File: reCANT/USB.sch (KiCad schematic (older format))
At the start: 15 parts, among them J1 USB_C_Receptacle_USB2.0, U1 USB3343, U10 DSC1001

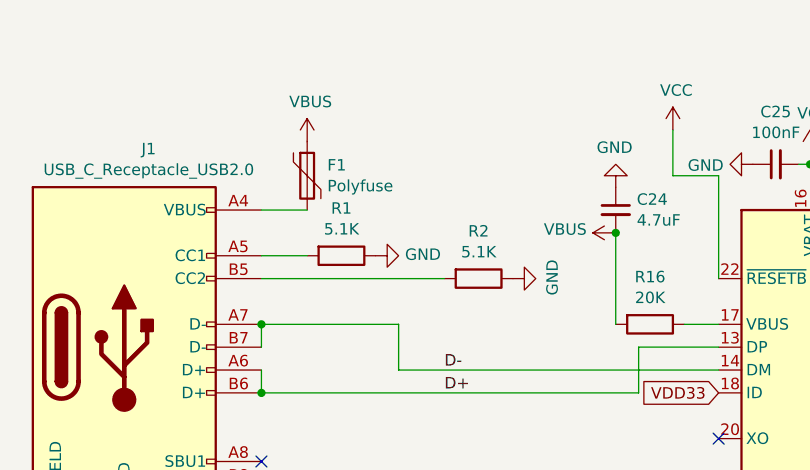
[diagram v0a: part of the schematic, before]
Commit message: Add LCSC part numbers for each component. Not that chipocalypse makes building this right now feasible...
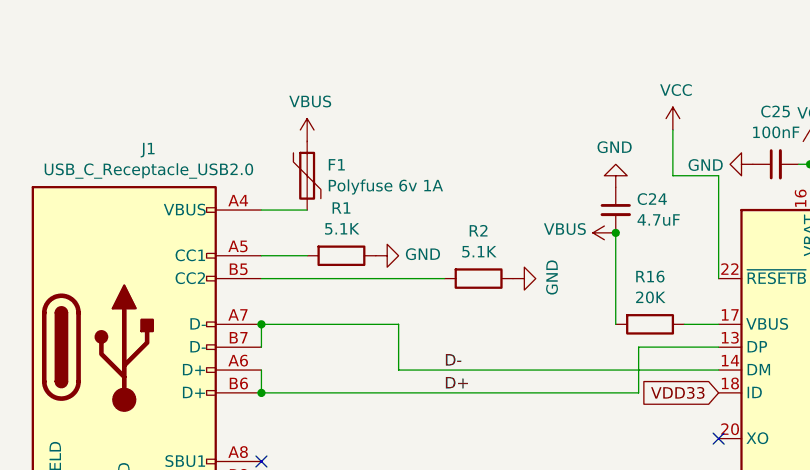
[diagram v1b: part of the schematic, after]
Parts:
- C1, C26, C27: LCSC (none) -> C28323
- C24: LCSC (none) -> C1779
- C25, C28, C29: LCSC (none) -> C49678
- F1: value Polyfuse -> Polyfuse 6v 1A; LCSC (none) -> C207022
- R1, R2: LCSC (none) -> C27834
- R16: LCSC (none) -> C4328
- R17: LCSC (none) -> C19006
- U1: LCSC (none) -> C112967
- U10: LCSC (none) -> C409249
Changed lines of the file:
@@
 P 2200 1200
 F 0 "F1" H 2288 1246 50  0000 L CNN
-F 1 "Polyfuse" H 2288 1155 50  0000 L CNN
+F 1 "Polyfuse 6v 1A" H 2288 1155 50  0000 L CNN
 F 2 "Capacitor_SMD:C_0805_2012Metric" H 2250 1000 50  0001 L CNN
 F 3 "~" H 2200 1200 50  0001 C CNN
+F 4 "C207022" H 2200 1200 50  0001 C CNN "LCSC"
 	1    2200 1200
 	1    0    0    -1
@@
 F 2 "Resistor_SMD:R_0805_2012Metric" V 2280 1550 50  0001 C CNN
 F 3 "~" H 2350 1550 50  0001 C CNN
+F 4 "C27834" V 2350 1550 50  0001 C CNN "LCSC"
 	1    2350 1550
 	0    1    1    0
@@
 F 2 "Resistor_SMD:R_0805_2012Metric" V 2880 1650 50  0001 C CNN
 F 3 "~" H 2950 1650 50  0001 C CNN
+F 4 "C27834" V 2950 1650 50  0001 C CNN "LCSC"
 	1    2950 1650
 	0    1    1    0
@@
 F 2 "Capacitor_SMD:C_0805_2012Metric" H 850 3050 50  0001 C CNN
 F 3 "~" H 850 3050 50  0001 C CNN
+F 4 "C28323" V 850 3050 50  0001 C CNN "LCSC"
 	1    850  3050
 	0    -1   -1   0
@@
 F 2 "Resistor_SMD:R_0805_2012Metric" V 3780 2850 50  0001 C CNN
 F 3 "~" H 3850 2850 50  0001 C CNN
+F 4 "C19006" V 3850 2850 50  0001 C CNN "LCSC"
 	1    3850 2850
 	0    1    1    0
@@
 F 2 "Capacitor_SMD:C_0805_2012Metric" H 3550 1350 50  0001 C CNN
 F 3 "~" H 3550 1350 50  0001 C CNN
+F 4 "C1779" H 3550 1350 50  0001 C CNN "LCSC"
 	1    3550 1350
 	1    0    0    -1
@@
 F 2 "Resistor_SMD:R_0805_2012Metric" V 3630 1850 50  0001 C CNN
 F 3 "~" H 3700 1850 50  0001 C CNN
+F 4 "C4328" V 3700 1850 50  0001 C CNN "LCSC"
 	1    3700 1850
 	0    1    1    0
@@
 F 2 "Capacitor_SMD:C_0805_2012Metric" H 4250 1150 50  0001 C CNN
 F 3 "~" H 4250 1150 50  0001 C CNN
+F 4 "C49678" V 4250 1150 50  0001 C CNN "LCSC"
 	1    4250 1150
 	0    -1   -1   0
@@
 F 2 "Capacitor_SMD:C_0805_2012Metric" H 4700 1050 50  0001 C CNN
 F 3 "~" H 4700 1050 50  0001 C CNN
+F 4 "C28323" V 4700 1050 50  0001 C CNN "LCSC"
 	1    4700 1050
 	0    -1   -1   0
@@
 F 2 "Capacitor_SMD:C_0805_2012Metric" H 5200 1200 50  0001 C CNN
 F 3 "~" H 5200 1200 50  0001 C CNN
+F 4 "C28323" V 5200 1200 50  0001 C CNN "LCSC"
 	1    5200 1200
 	0    1    1    0
@@
 F 2 "Package_DFN_QFN:QFN-24-1EP_4x4mm_P0.5mm_EP2.6x2.6mm" H 5100 2350 50  0001 C CNN
 F 3 "http://ww1.microchip.com/downloads/en/DeviceDoc/334x.pdf" H 5100 2450 50  0001 C CNN
+F 4 "C112967" H 4600 2150 50  0001 C CNN "LCSC"
 	1    4600 2150
 	1    0    0    -1
@@
 F 2 "DSC1001:Oscillator_SMD_Microchip_DSC1001-4Pin_2.5x2.0mm" H 2700 3350 50  0001 C CNN
 F 3 "https://abracon.com/Oscillators/ASDMB.pdf" H 3000 3800 50  0001 C CNN
+F 4 "C409249" H 2700 3350 50  0001 C CNN "LCSC"
 	1    2700 3350
 	1    0    0    -1
@@
 F 2 "Capacitor_SMD:C_0805_2012Metric" H 5750 1500 50  0001 C CNN
 F 3 "~" H 5750 1500 50  0001 C CNN
+F 4 "C49678" H 5750 1500 50  0001 C CNN "LCSC"
 	1    5750 1500
 	1    0    0    -1
@@
 F 2 "Capacitor_SMD:C_0805_2012Metric" H 2600 2900 50  0001 C CNN
 F 3 "~" H 2600 2900 50  0001 C CNN
+F 4 "C49678" V 2600 2900 50  0001 C CNN "LCSC"
 	1    2600 2900
 	0    1    1    0

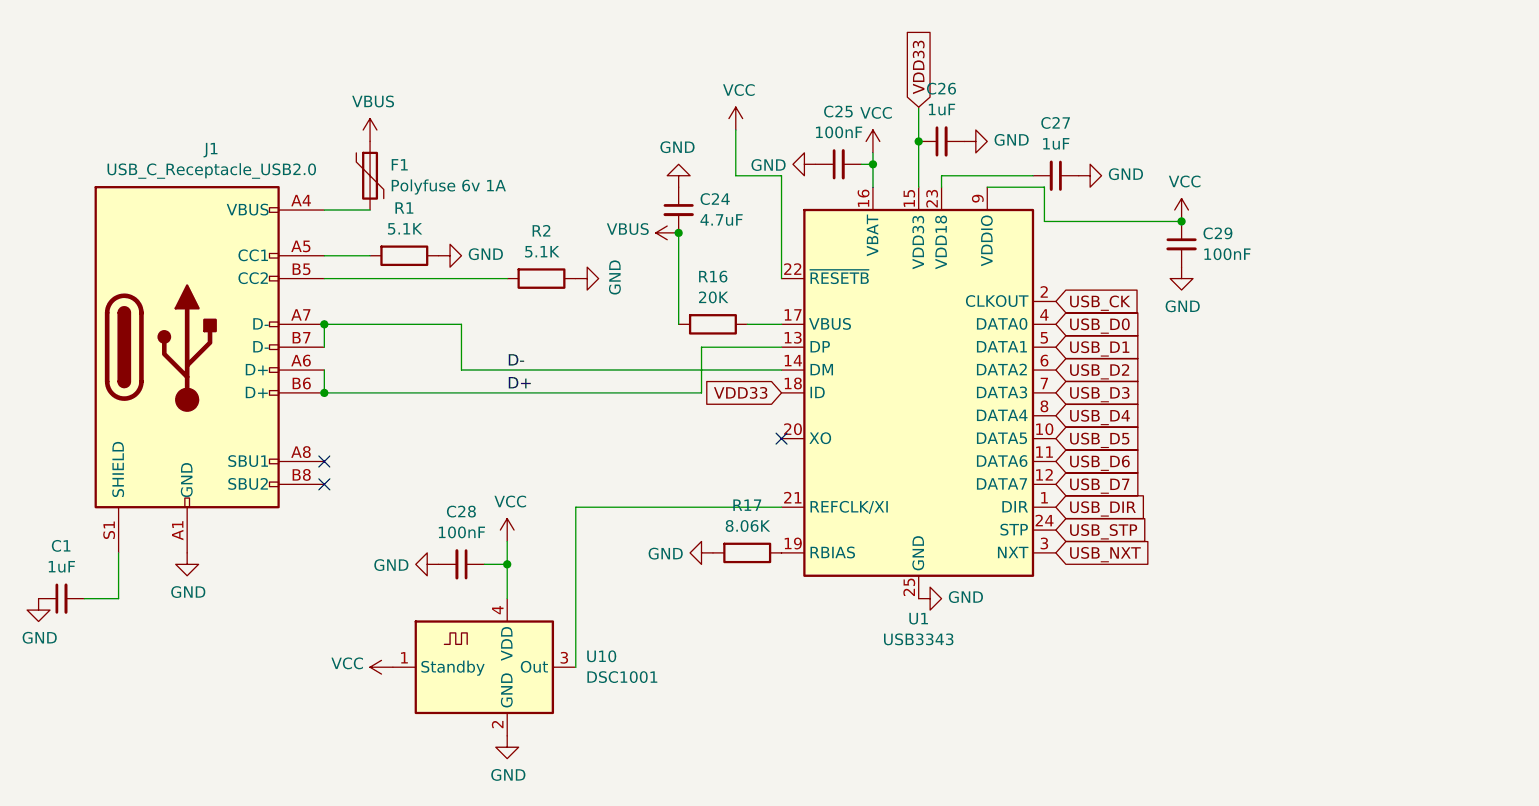
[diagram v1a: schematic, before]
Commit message: Added test points for debugging USB. Fixed impedence on USB traces to be correct for JLCPCBs JLC7628 buildup
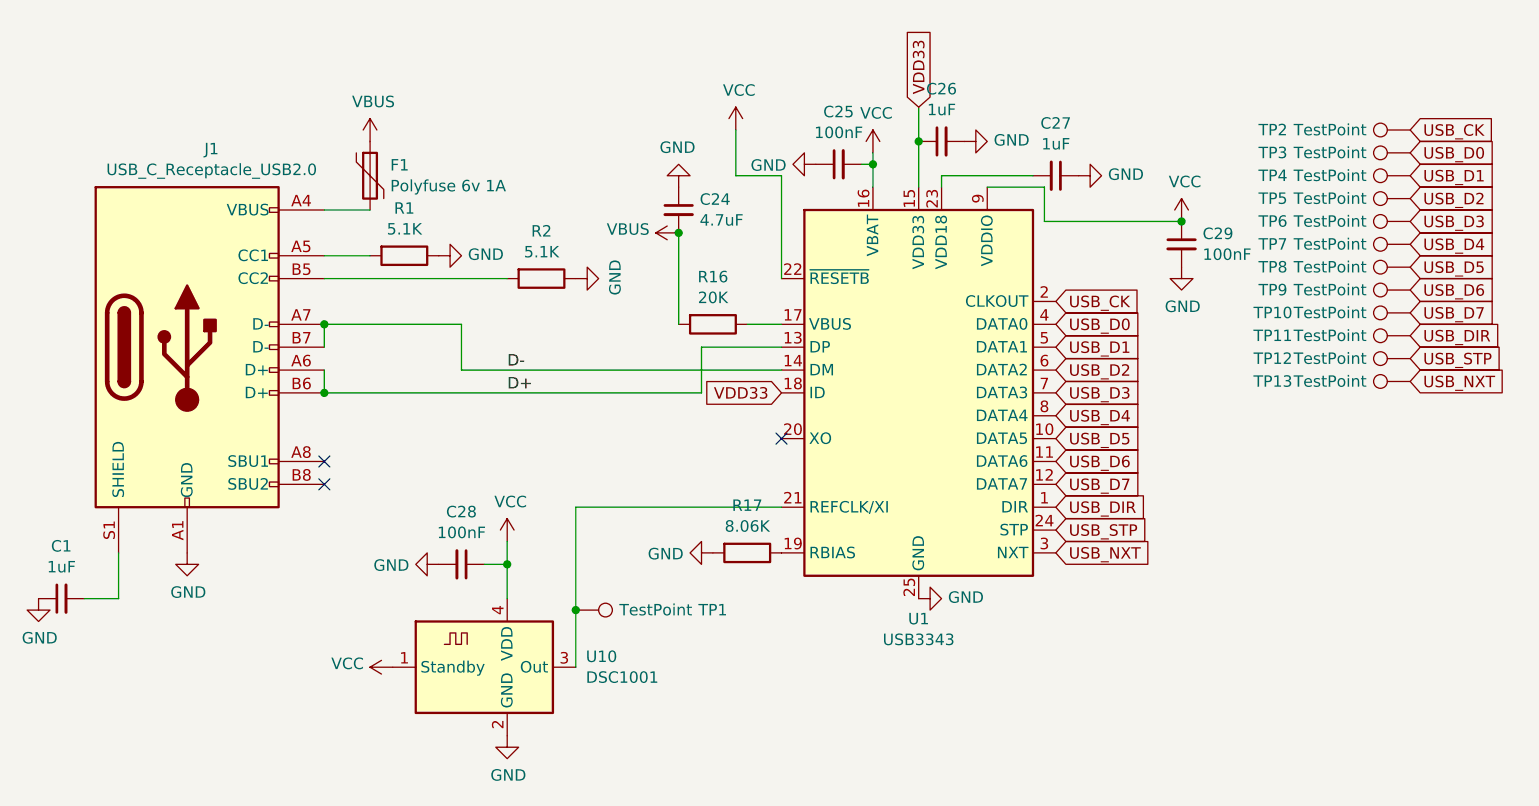
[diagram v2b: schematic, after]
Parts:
- added TP1, TP10, TP11, TP12, TP13, TP2, TP3, TP4, TP5, TP6, TP7, TP8, TP9: TestPoint, TestPoint:TestPoint_Pad_D1.0mm, symbol Connector:TestPoint
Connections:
- net USB_CK: now also TP2.1
- net USB_D0: now also TP3.1
- net USB_D1: now also TP4.1
- net USB_D2: now also TP5.1
- net USB_D3: now also TP6.1
- net USB_D4: now also TP7.1
- net USB_D5: now also TP8.1
- net USB_D6: now also TP9.1
- net USB_D7: now also TP10.1
- net USB_DIR: now also TP11.1
- net USB_NXT: now also TP13.1
- net USB_STP: now also TP12.1
- net at U1.21 (REFCLK/XI), U10.3 (Out): now also TP1.1
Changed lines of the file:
@@
 $EndComp
 Wire Wire Line
-	3100 3350 3100 2650
+	3100 3350 3100 3100
 Wire Wire Line
 	3100 2650 4000 2650
@@
 $EndComp
 Wire Wire Line
-	5750 1400 5150 1400
-Wire Wire Line
 	5150 1400 5150 1250
 Wire Wire Line
@@
 	1    0    0    -1
 $EndComp
+Text GLabel 6750 1000 2    50   Input ~ 0
+USB_CK
+Text GLabel 6750 1100 2    50   Input ~ 0
+USB_D0
+Text GLabel 6750 1200 2    50   Input ~ 0
+USB_D1
+Text GLabel 6750 1300 2    50   Input ~ 0
+USB_D2
+Text GLabel 6750 1400 2    50   Input ~ 0
+USB_D3
+Text GLabel 6750 1500 2    50   Input ~ 0
+USB_D4
+Text GLabel 6750 1600 2    50   Input ~ 0
+USB_D5
+Text GLabel 6750 1700 2    50   Input ~ 0
+USB_D6
+Text GLabel 6750 1800 2    50   Input ~ 0
+USB_D7
+Text GLabel 6750 1900 2    50   Input ~ 0
+USB_DIR
+Text GLabel 6750 2000 2    50   Input ~ 0
+USB_STP
+Text GLabel 6750 2100 2    50   Input ~ 0
+USB_NXT
+$Comp
+L Connector:TestPoint TP2
+U 1 1 623221AE
+P 6750 1000
+F 0 "TP2" V 6750 1600 50  0000 C CNN
+F 1 "TestPoint" V 6750 1350 50  0000 C CNN
+F 2 "TestPoint:TestPoint_Pad_D1.0mm" H 6950 1000 50  0001 C CNN
+F 3 "~" H 6950 1000 50  0001 C CNN
+	1    6750 1000
+	0    -1   -1   0
+$EndComp
+Wire Wire Line
+	5150 1400 5750 1400
+$Comp
+L Connector:TestPoint TP3
+U 1 1 62325BCC
+P 6750 1100
+F 0 "TP3" V 6750 1700 50  0000 C CNN
+F 1 "TestPoint" V 6750 1450 50  0000 C CNN
+F 2 "TestPoint:TestPoint_Pad_D1.0mm" H 6950 1100 50  0001 C CNN
+F 3 "~" H 6950 1100 50  0001 C CNN
+	1    6750 1100
+	0    -1   -1   0
+$EndComp
+$Comp
+L Connector:TestPoint TP4
+U 1 1 62325E52
+P 6750 1200
+F 0 "TP4" V 6750 1800 50  0000 C CNN
+F 1 "TestPoint" V 6750 1550 50  0000 C CNN
+F 2 "TestPoint:TestPoint_Pad_D1.0mm" H 6950 1200 50  0001 C CNN
+F 3 "~" H 6950 1200 50  0001 C CNN
+	1    6750 1200
+	0    -1   -1   0
+$EndComp
+$Comp
+L Connector:TestPoint TP5
+U 1 1 623260E2
+P 6750 1300
+F 0 "TP5" V 6750 1900 50  0000 C CNN
+F 1 "TestPoint" V 6750 1650 50  0000 C CNN
+F 2 "TestPoint:TestPoint_Pad_D1.0mm" H 6950 1300 50  0001 C CNN
+F 3 "~" H 6950 1300 50  0001 C CNN
+	1    6750 1300
+	0    -1   -1   0
+$EndComp
+$Comp
+L Connector:TestPoint TP6
+U 1 1 6232637C
+P 6750 1400
+F 0 "TP6" V 6750 2000 50  0000 C CNN
+F 1 "TestPoint" V 6750 1750 50  0000 C CNN
+F 2 "TestPoint:TestPoint_Pad_D1.0mm" H 6950 1400 50  0001 C CNN
+F 3 "~" H 6950 1400 50  0001 C CNN
+	1    6750 1400
+	0    -1   -1   0
+$EndComp
+$Comp
+L Connector:TestPoint TP7
+U 1 1 62326612
+P 6750 1500
+F 0 "TP7" V 6750 2100 50  0000 C CNN
+F 1 "TestPoint" V 6750 1850 50  0000 C CNN
+F 2 "TestPoint:TestPoint_Pad_D1.0mm" H 6950 1500 50  0001 C CNN
+F 3 "~" H 6950 1500 50  0001 C CNN
+	1    6750 1500
+	0    -1   -1   0
+$EndComp
+$Comp
+L Connector:TestPoint TP8
+U 1 1 623268B2
+P 6750 1600
+F 0 "TP8" V 6750 2200 50  0000 C CNN
+F 1 "TestPoint" V 6750 1950 50  0000 C CNN
+F 2 "TestPoint:TestPoint_Pad_D1.0mm" H 6950 1600 50  0001 C CNN
+F 3 "~" H 6950 1600 50  0001 C CNN
+	1    6750 1600
+	0    -1   -1   0
+$EndComp
+$Comp
+L Connector:TestPoint TP9
+U 1 1 62326B5C
+P 6750 1700
+F 0 "TP9" V 6750 2300 50  0000 C CNN
+F 1 "TestPoint" V 6750 2050 50  0000 C CNN
+F 2 "TestPoint:TestPoint_Pad_D1.0mm" H 6950 1700 50  0001 C CNN
+F 3 "~" H 6950 1700 50  0001 C CNN
+	1    6750 1700
+	0    -1   -1   0
+$EndComp
+$Comp
+L Connector:TestPoint TP10
+U 1 1 62326E10
+P 6750 1800
+F 0 "TP10" V 6750 2400 50  0000 C CNN
+F 1 "TestPoint" V 6750 2150 50  0000 C CNN
+F 2 "TestPoint:TestPoint_Pad_D1.0mm" H 6950 1800 50  0001 C CNN
+F 3 "~" H 6950 1800 50  0001 C CNN
+	1    6750 1800
+	0    -1   -1   0
+$EndComp
+$Comp
+L Connector:TestPoint TP11
+U 1 1 623270CE
+P 6750 1900
+F 0 "TP11" V 6750 2500 50  0000 C CNN
+F 1 "TestPoint" V 6750 2250 50  0000 C CNN
+F 2 "TestPoint:TestPoint_Pad_D1.0mm" H 6950 1900 50  0001 C CNN
+F 3 "~" H 6950 1900 50  0001 C CNN
+	1    6750 1900
+	0    -1   -1   0
+$EndComp
+$Comp
+L Connector:TestPoint TP12
+U 1 1 62327396
+P 6750 2000
+F 0 "TP12" V 6750 2600 50  0000 C CNN
+F 1 "TestPoint" V 6750 2350 50  0000 C CNN
+F 2 "TestPoint:TestPoint_Pad_D1.0mm" H 6950 2000 50  0001 C CNN
+F 3 "~" H 6950 2000 50  0001 C CNN
+	1    6750 2000
+	0    -1   -1   0
+$EndComp
+$Comp
+L Connector:TestPoint TP13
+U 1 1 62327676
+P 6750 2100
+F 0 "TP13" V 6750 2700 50  0000 C CNN
+F 1 "TestPoint" V 6750 2450 50  0000 C CNN
+F 2 "TestPoint:TestPoint_Pad_D1.0mm" H 6950 2100 50  0001 C CNN
+F 3 "~" H 6950 2100 50  0001 C CNN
+	1    6750 2100
+	0    -1   -1   0
+$EndComp
+$Comp
+L Connector:TestPoint TP1
+U 1 1 62327960
+P 3100 3100
+F 0 "TP1" V 3100 3700 50  0000 C CNN
+F 1 "TestPoint" V 3100 3450 50  0000 C CNN
+F 2 "TestPoint:TestPoint_Pad_D1.0mm" H 3300 3100 50  0001 C CNN
+F 3 "~" H 3300 3100 50  0001 C CNN
+	1    3100 3100
+	0    1    1    0
+$EndComp
+Connection ~ 3100 3100
+Wire Wire Line
+	3100 3100 3100 2650
 $EndSCHEMATC
